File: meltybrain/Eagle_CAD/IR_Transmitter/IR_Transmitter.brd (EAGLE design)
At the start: 160 x 100 mm, 0 parts

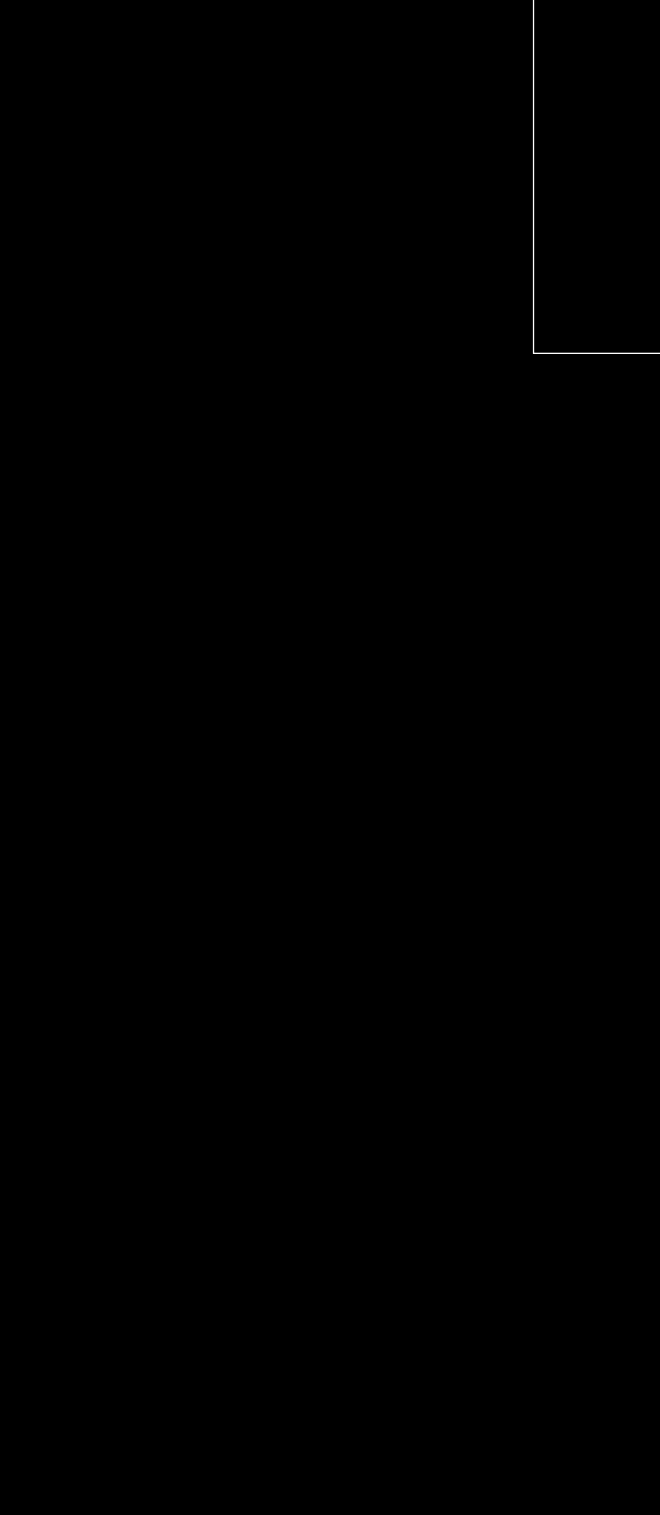
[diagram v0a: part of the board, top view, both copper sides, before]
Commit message: Reverse polarity protection
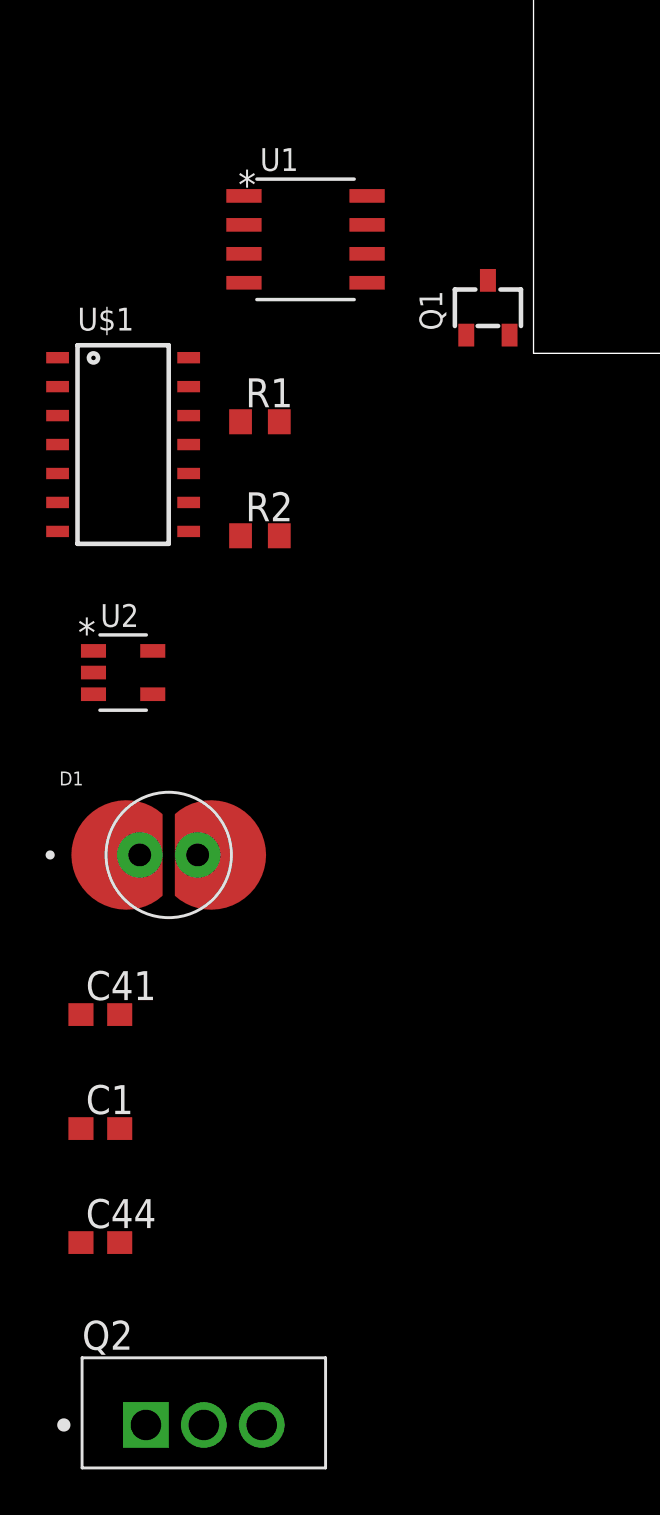
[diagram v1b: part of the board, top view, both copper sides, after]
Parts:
- added C1: 100p, rcl:C0603
- added C41: 1u, rcl:C0603
- added C44: 2.2u, rcl:C0603
- added D1: SFH_4544, EmitterParts:DIO_SFH_4544
- added Q1: BSS806N, RoboJackets-Discrete:SOT-23-3
- added Q2: FQP47P06, EmitterParts:TO254P1067X483X2286-3
- added R1: 6.8, rcl:R0603
- added R2: 500, rcl:R0603
- added U$1: ATTINY84, EmitterParts:SOIC-14
- added U1: LMH6612MAX/NOPB, Hocki_Library:8-SOIC
- added U2: AP2210K-5.0TRG1, Hocki_Library:SOT-23-5
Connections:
- new net +5V: C44.1, D1.A, U$1.1, U1.8, U2.5
- new net 9V: Q2.2
- new net GND: C1.2, C41.2, C44.2, Q2.1, R1.1, R2.1, U$1.14, U1.4, U1.5, U1.6, U2.2
- new net N$1: Q1.2, R1.2, U1.2
- new net N$2: Q1.1, U1.1
- new net N$3: R2.2, U1.7
- new net N$4: U$1.8, U1.3
- new net N$5: D1.C, Q1.3
- new net N$6: C1.1, U2.4
- new net N$7: C41.1, Q2.3, U2.1, U2.3

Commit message: Connector progress
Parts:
- added CN1: (no value), Hocki_Library:JST-PH-2-SMT-RA
- added J1: 4PIN-0353620450, RoboJackets-Connectors:0353620450
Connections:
- new net N$8: U$1.7
- new net N$9: U$1.4
- net 9V: now also CN1.1, CN1.NC1, CN1.NC2
- net GND: now also CN1.2
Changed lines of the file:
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@@
 <attribute name="VALUE" x="-19.773140625" y="-49.203190625" size="1.27" layer="27" align="top-left"/>
+</element>
+<element name="CN1" library="Hocki_Library" package="JST-PH-2-SMT-RA" value="" x="-26" y="-42" smashed="yes">
+<attribute name="NAME" x="-28.54" y="-38.19" size="1.27" layer="25" font="vector"/>
+<attribute name="VALUE" x="-28.54" y="-49.62" size="1.27" layer="27" font="vector"/>
+</element>
+<element name="J1" library="RoboJackets-Connectors" package="0353620450" value="4PIN-0353620450" x="-25" y="-56" smashed="yes">
+<attribute name="DKPN" value="WM18922-ND" x="-25" y="-56" size="1.778" layer="27" display="off"/>
+<attribute name="NAME" x="-28.99" y="-52.48" size="1" layer="25" font="vector"/>
+<attribute name="VALUE" x="-29" y="-59.5" size="1" layer="27" font="vector" align="top-left"/>
 </element>
 </elements>
@@
 <contactref element="C44" pad="2"/>
 <contactref element="Q2" pad="1"/>
+<contactref element="CN1" pad="2"/>
+<wire x1="-17" y1="-47" x2="-27" y2="-45.7" width="0" layer="19" extent="1-1"/>
 <wire x1="-18.15" y1="-39" x2="-17" y2="-47" width="0" layer="19" extent="1-1"/>
 <wire x1="-18.15" y1="-34" x2="-18.15" y2="-39" width="0" layer="19" extent="1-1"/>
@@
 <signal name="9V">
 <contactref element="Q2" pad="2"/>
+<contactref element="CN1" pad="1"/>
+<contactref element="CN1" pad="NC2"/>
+<contactref element="CN1" pad="NC1"/>
+<wire x1="-22.6" y1="-40.5" x2="-25" y2="-45.7" width="0" layer="19" extent="1-1"/>
+<wire x1="-29.4" y1="-40.5" x2="-22.6" y2="-40.5" width="0" layer="19" extent="1-1"/>
+<wire x1="-14.46" y1="-47" x2="-22.6" y2="-40.5" width="0" layer="19" extent="1-1"/>
+</signal>
+<signal name="N$8">
+<contactref element="U$1" pad="7"/>
+</signal>
+<signal name="N$9">
+<contactref element="U$1" pad="4"/>
 </signal>
 </signals>

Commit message: Connector progress
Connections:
- removed net N$4: U$1.8, U1.3
- removed net N$8: U$1.7
- removed net N$9: U$1.4
- new net MISO: J1.2, U$1.8, U1.3
- new net MOSI: J1.1, U$1.7
- new net SCK: J1.3, U$1.9
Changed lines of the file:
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@@
 <wire x1="-7.3" y1="6.905" x2="-20.875" y2="-0.19" width="0" layer="19" extent="1-1"/>
-</signal>
-<signal name="N$4">
-<contactref element="U$1" pad="8"/>
-<contactref element="U1" pad="3"/>
-<wire x1="-12.7" y1="4.365" x2="-15.125" y2="-7.81" width="0" layer="19" extent="1-1"/>
 </signal>
 <signal name="N$5">
@@
 <wire x1="-14.46" y1="-47" x2="-22.6" y2="-40.5" width="0" layer="19" extent="1-1"/>
 </signal>
-<signal name="N$8">
+<signal name="MOSI">
 <contactref element="U$1" pad="7"/>
+<contactref element="J1" pad="1"/>
+<wire x1="-20.875" y1="-7.81" x2="-27" y2="-56" width="0" layer="19" extent="1-1"/>
 </signal>
-<signal name="N$9">
-<contactref element="U$1" pad="4"/>
+<signal name="SCK">
+<contactref element="U$1" pad="9"/>
+<contactref element="J1" pad="3"/>
+<wire x1="-15.125" y1="-6.54" x2="-23" y2="-56" width="0" layer="19" extent="1-1"/>
+</signal>
+<signal name="MISO">
+<contactref element="U$1" pad="8"/>
+<contactref element="U1" pad="3"/>
+<contactref element="J1" pad="2"/>
+<wire x1="-15.125" y1="-7.81" x2="-25" y2="-56" width="0" layer="19" extent="1-1"/>
+<wire x1="-12.7" y1="4.365" x2="-15.125" y2="-7.81" width="0" layer="19" extent="1-1"/>
 </signal>
 </signals>

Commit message: Schematic Finished, Board Routed
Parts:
- added C2: 0.1u, rcl:C0603
- J1: value 4PIN-0353620450 -> AVR_SPI_PROG_3X2NS; device RoboJackets-Connectors:0353620450 -> SparkFun-Connectors:2X3-NS
- Q2: value FQP47P06 -> FDN352AP; device EmitterParts:TO254P1067X483X2286-3 -> EmitterParts:SSOT-3
- moved Q2 74.3 mm to (13.0, 21.0)
- moved J1 73.5 mm to (4.20, 11.4), turned to 90 degrees
- moved C44 72.3 mm to (18.3, 22.9), turned to 90 degrees
- moved CN1 69.4 mm to (4.70, 20.2), turned to 90 degrees
- moved C1 61.5 mm to (18.3, 14.9), turned to 270 degrees
- moved D1 58.7 mm to (25.0, 20.0), turned to 180 degrees
- moved C41 56.0 mm to (15.7, 14.9), turned to 270 degrees
- moved R2 49.6 mm to (35.8, 5.40), turned to 270 degrees
- moved U2 48.1 mm to (17.0, 19.0)
- moved R1 47.5 mm to (32.0, 14.8)
- moved U1 41.0 mm to (31.0, 4.00)
- moved U$1 39.3 mm to (20.0, 6.00)
- moved Q1 37.8 mm to (31.9, 18.8)
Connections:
- new net OUT: U$1.5, U1.3
- new net RST: J1.5, U$1.4
- net +5V: now also C2.1, J1.2
- net 9V: now also Q2.3; no longer CN1.NC1, CN1.NC2, Q2.2
- net GND: now also C2.2, J1.6
- net MISO: now also J1.1; no longer J1.2, U1.3
- net MOSI: now also J1.4; no longer J1.1
- net N$7: now also Q2.2; no longer Q2.3
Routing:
- net +5V: track 0.00 -> 65.2 mm
- net GND: track 0.00 -> 27.4 mm, vias 0 -> 14
- net SCK: track 0.00 -> 21.1 mm
- net MISO: track 0.00 -> 20.6 mm
- net MOSI: track 0.00 -> 18.0 mm
- net N$1: track 0.00 -> 15.0 mm
- net RST: track 0.00 -> 14.9 mm
- net N$2: track 0.00 -> 12.8 mm
- net OUT: track 0.00 -> 11.7 mm
- net N$7: track 0.00 -> 6.87 mm
- net N$5: track 0.00 -> 5.63 mm
- net 9V: track 0.00 -> 4.97 mm
- net N$6: track 0.00 -> 2.30 mm
- net N$3: track 0.00 -> 2.12 mm
- added copper zone on layer 16, net GND
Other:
- board size 160 x 100 mm -> 41 x 31 mm

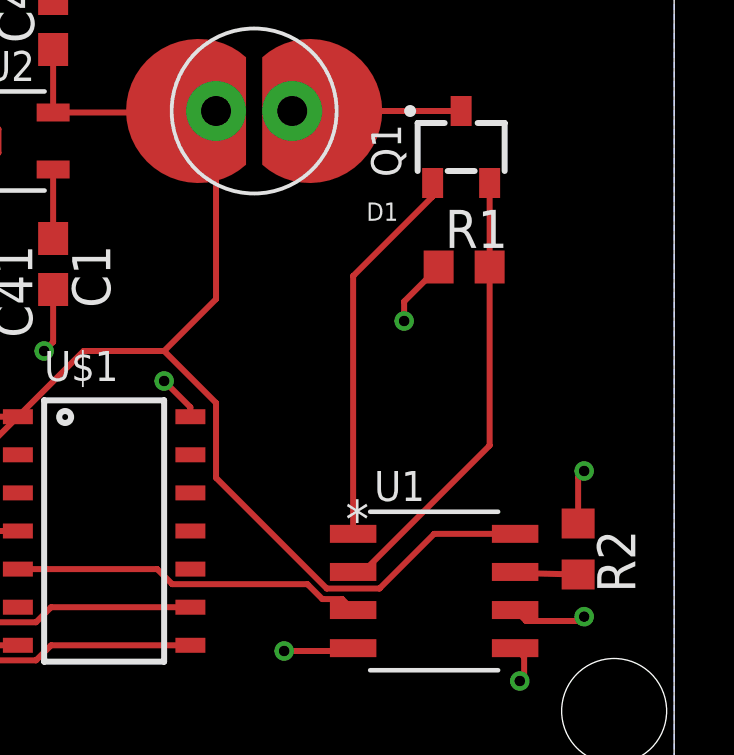
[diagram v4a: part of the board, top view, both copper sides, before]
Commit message: Replaced resistor R1 with 1.5 ohm 0402 Resistor
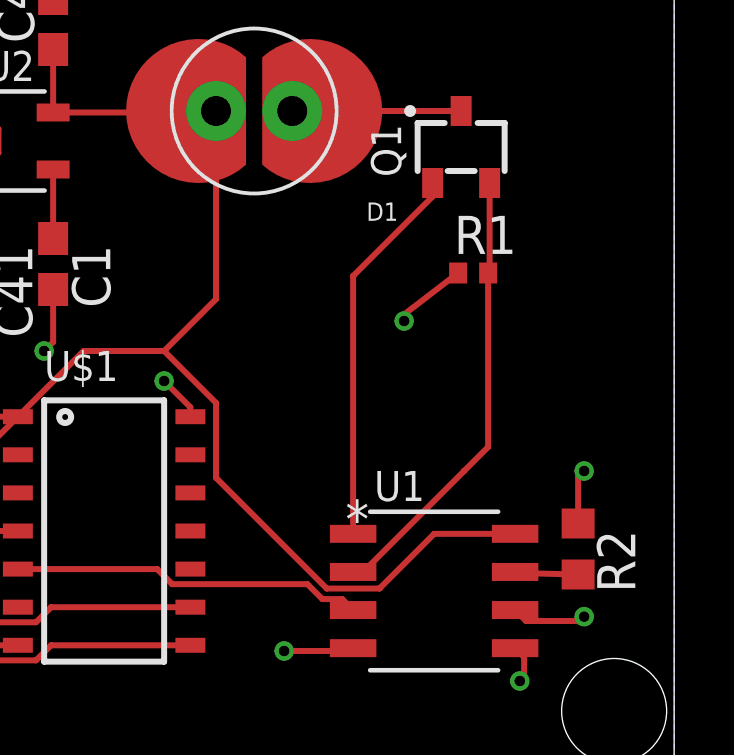
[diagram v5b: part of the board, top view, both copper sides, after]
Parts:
- R1: value 6.8 -> 1.5; device rcl:R0603 -> rcl:R0402
- moved R1 0.36 mm to (32.3, 14.6)
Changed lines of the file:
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@@
 <attribute name="VALUE" x="29" y="1" size="1" layer="27" font="vector" rot="SR0" align="top-left"/>
 </element>
-<element name="R1" library="rcl" library_urn="urn:adsk.eagle:library:334" package="R0603" package3d_urn="urn:adsk.eagle:package:23555/3" value="6.8" x="32" y="14.8" smashed="yes">
-<attribute name="NAME" x="31.365" y="15.435" size="1.27" layer="25"/>
-<attribute name="POPULARITY" value="77" x="32" y="14.8" size="1.778" layer="27" display="off"/>
-<attribute name="SPICEPREFIX" value="R" x="32" y="14.8" size="1.778" layer="27" display="off"/>
-<attribute name="VALUE" x="31.365" y="12.895" size="1.27" layer="27"/>
+<element name="R1" library="rcl" library_urn="urn:adsk.eagle:library:334" package="R0402" package3d_urn="urn:adsk.eagle:package:23547/3" value="1.5" x="32.3" y="14.6" smashed="yes">
+<attribute name="NAME" x="31.665" y="15.235" size="1.27" layer="25"/>
+<attribute name="POPULARITY" value="34" x="32.3" y="14.6" size="1.778" layer="27" display="off"/>
+<attribute name="SPICEPREFIX" value="R" x="32.3" y="14.6" size="1.778" layer="27" display="off"/>
+<attribute name="VALUE" x="31.665" y="12.695" size="1.27" layer="27"/>
 </element>
 <element name="R2" library="rcl" library_urn="urn:adsk.eagle:library:334" package="R0603" package3d_urn="urn:adsk.eagle:package:23555/3" value="500" x="35.8" y="5.4" smashed="yes" rot="R270">
@@
 <contactref element="Q1" pad="2"/>
 <contactref element="R1" pad="2"/>
-<wire x1="32.85" y1="17.6" x2="32.85" y2="14.8" width="0.2" layer="1"/>
-<wire x1="32.85" y1="14.8" x2="32.85" y2="8.85" width="0.2" layer="1"/>
 <wire x1="28.635" y1="4.635" x2="28.3" y2="4.635" width="0.2" layer="1"/>
-<wire x1="32.85" y1="8.85" x2="28.635" y2="4.635" width="0.2" layer="1"/>
+<wire x1="32" y1="8" x2="28.635" y2="4.635" width="0.2" layer="1"/>
+<wire x1="32.85" y1="17.6" x2="32.85" y2="14.65" width="0.2" layer="1"/>
+<wire x1="32.85" y1="14.65" x2="32.8" y2="14.6" width="0.2" layer="1"/>
+<wire x1="32.8" y1="14.6" x2="32.8" y2="8.8" width="0.2" layer="1"/>
+<wire x1="32.8" y1="8.8" x2="32" y2="8" width="0.2" layer="1"/>
 </signal>
 <signal name="N$2">
@@
 <wire x1="0.06" y1="13.94" x2="0" y2="14" width="0.2" layer="16"/>
 <via x="0" y="14" extent="1-16" drill="0.35"/>
-<wire x1="31.15" y1="14.8" x2="30" y2="13.65" width="0.2" layer="1"/>
-<wire x1="30" y1="13.65" x2="30" y2="13" width="0.2" layer="1"/>
+<wire x1="31.8" y1="14.6" x2="30" y2="13.22" width="0.2" layer="1"/>
+<wire x1="30" y1="13.22" x2="30" y2="13" width="0.2" layer="1"/>
 <via x="30" y="13" extent="1-16" drill="0.35"/>
 <wire x1="35.8" y1="6.25" x2="35.8" y2="7.8" width="0.2" layer="1"/>
